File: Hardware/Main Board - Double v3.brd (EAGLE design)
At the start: 124.5 x 73.7 mm, 134 parts, among them J1 MICROMOD-2222-C, J10 MICRO-SD-PUSH-PUSH-EXT-PIN, J2 Vertical Qwiic Connector, J4 QWIIC_RIGHT_ANGLE, J5 CORTEX_JTAG_DEBUG_MINIMUM_PTH, J6 MICROMOD_FUNCTION_MAIN, J7 MICROMOD_FUNCTION_MAIN, Q1 3.1A/30V/105mΩ, Q2 20V/4.2A/52mΩ/1.4W, U1 STG3856QTR, U2 MCP73831, U3 ESD Diode, U4 AP7347DQ-33W5-7K-3.3V, U5 AP7361C-33

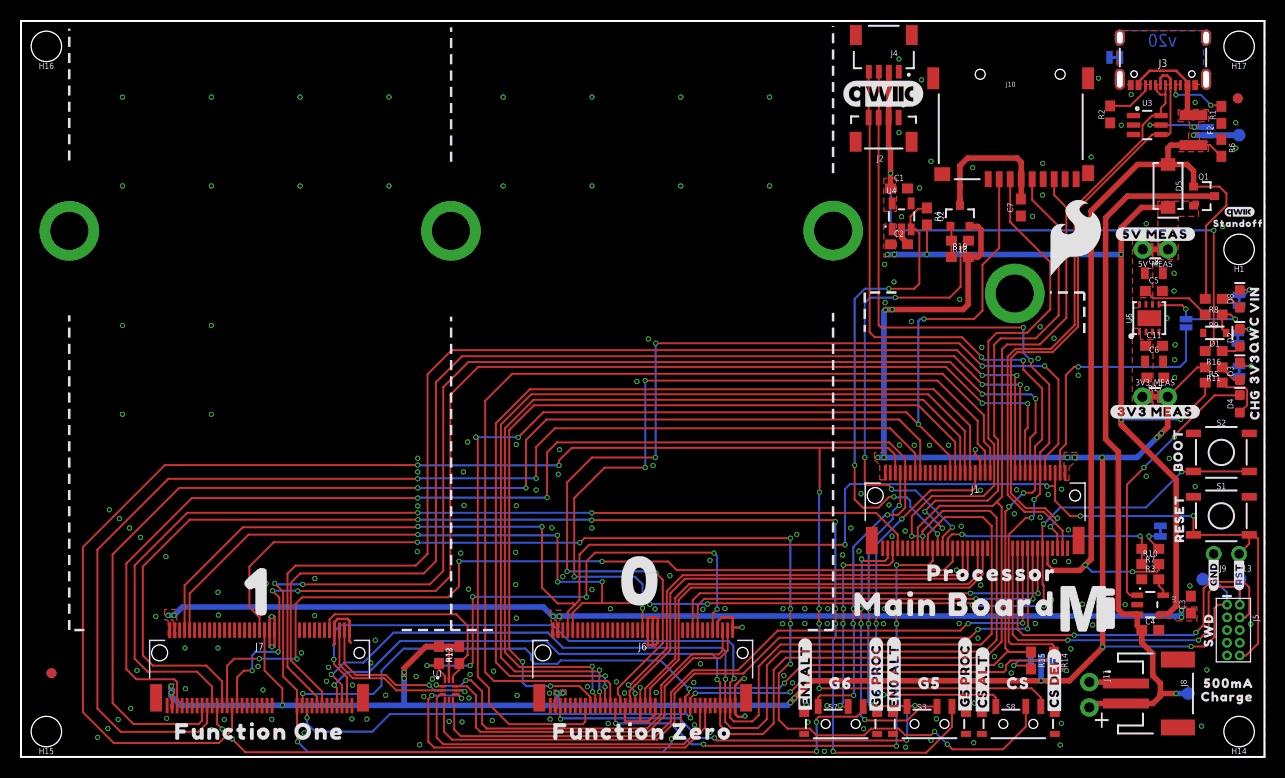
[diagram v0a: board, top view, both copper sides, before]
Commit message: Removes old designs, updates polygons
* Updates silk
* Uses VIN as power supply to battery charger
* Fixes PCH Mosfet
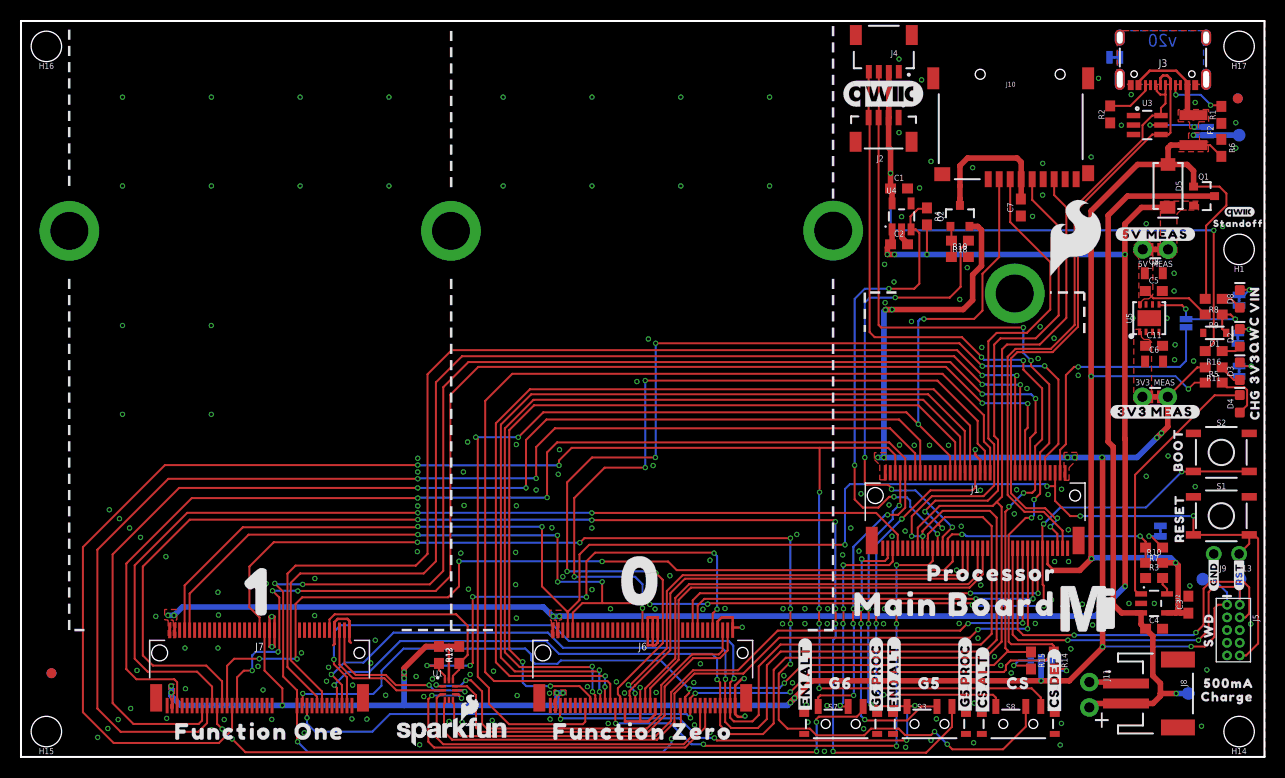
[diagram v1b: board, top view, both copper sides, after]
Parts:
- removed R17: 2.0M, SparkFun-Resistors:0603
- added U$44: (no value), SparkFun-Aesthetics:SFE_LOGO_NAME_FLAME_.1
- moved R10 0.40 mm to (113.4, 19.4)
- moved C4 0.40 mm to (113.4, 12.8)
- moved U2 0.40 mm to (113.4, 15.4)
- moved R3 0.40 mm to (113.4, 17.9)
- moved R7 0.40 mm to (113.4, 21.0)
- moved C3 0.25 mm to (116.8, 15.2)
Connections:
- net I2C_SDA1-PROCESSOR/!SD_DISABLE! renamed I2C_SDA1-PROCESSOR/!SD_ENABLE!
- net 3.3V: no longer R19.2
- net 3V3_MEAS: no longer R17.2
- net GND: now also R19.2; no longer R17.1
- net VCC: no longer C3.1, R5.1, U2.4
- net VIN: now also C3.1, R5.1, U2.4
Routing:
- net VIN: track 91.0 -> 112.8 mm, vias 3 -> 5
- net VCC: track 187.3 -> 168.5 mm, vias 12 -> 9
- net 3.3V_QWIIC: track 62.0 -> 63.6 mm
- net N$14: track 27.0 -> 26.1 mm, vias 2 -> 0
- net 3.3V: track 236.7 -> 236.2 mm
- net GND: vias 218 -> 220
- removed copper zone on layer 1, net 3.3V_QWIIC

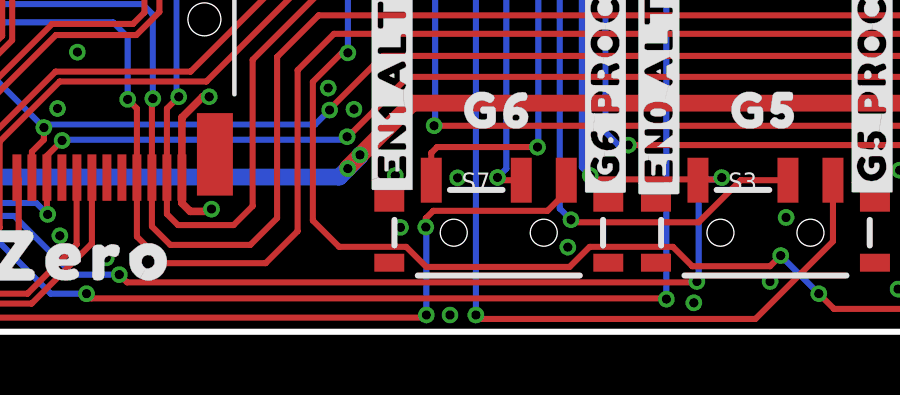
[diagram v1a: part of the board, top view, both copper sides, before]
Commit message: Fixes airwire
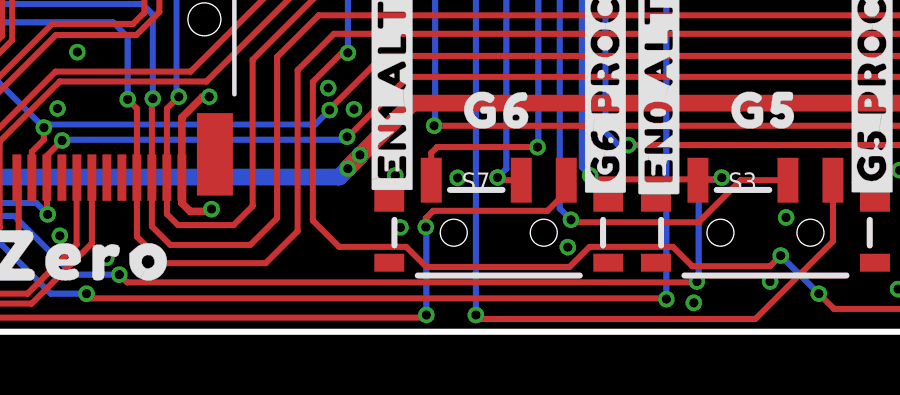
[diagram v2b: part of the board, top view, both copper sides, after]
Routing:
- net GND: vias 220 -> 219
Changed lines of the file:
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@@
 <layer number="20" name="Dimension" color="15" fill="1" visible="yes" active="yes"/>
 <layer number="21" name="tPlace" color="16" fill="1" visible="yes" active="yes"/>
-<layer number="22" name="bPlace" color="14" fill="1" visible="no" active="yes"/>
-<layer number="23" name="tOrigins" color="15" fill="1" visible="no" active="yes"/>
+<layer number="22" name="bPlace" color="14" fill="1" visible="yes" active="yes"/>
+<layer number="23" name="tOrigins" color="15" fill="1" visible="yes" active="yes"/>
 <layer number="24" name="bOrigins" color="15" fill="1" visible="yes" active="yes"/>
 <layer number="25" name="tNames" color="7" fill="1" visible="no" active="yes"/>
@@
 <layer number="39" name="tKeepout" color="4" fill="11" visible="no" active="yes"/>
 <layer number="40" name="bKeepout" color="1" fill="11" visible="no" active="yes"/>
-<layer number="41" name="tRestrict" color="4" fill="10" visible="yes" active="yes"/>
+<layer number="41" name="tRestrict" color="4" fill="10" visible="no" active="yes"/>
 <layer number="42" name="bRestrict" color="1" fill="10" visible="no" active="yes"/>
 <layer number="43" name="vRestrict" color="2" fill="10" visible="no" active="yes"/>
@@
 <via x="104.14" y="3.3528" extent="1-16" drill="0.3048"/>
 <via x="88.5444" y="0.9652" extent="1-16" drill="0.3048"/>
-<via x="80.4164" y="0.5588" extent="1-16" drill="0.3048"/>
 <via x="80.6704" y="5.1308" extent="1-16" drill="0.3048"/>
 <via x="39.6707875" y="20.5486" extent="1-16" drill="0.3048"/>
@@
 <via x="94.7166" y="48.9712" extent="1-16" drill="0.3048"/>
 <via x="113.4364" y="15.367" extent="1-16" drill="0.3048"/>
-<wire x1="80.4164" y1="0.5588" x2="78.7654" y2="3.4798" width="0" layer="19" extent="1-1"/>
 </signal>
 <signal name="V_BATT" class="1">
